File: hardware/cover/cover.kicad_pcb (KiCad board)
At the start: 2 copper layers, 35.5 x 41 mm, 5 parts, among them P101 CONN_02X03, SW101 SW_DIP_4

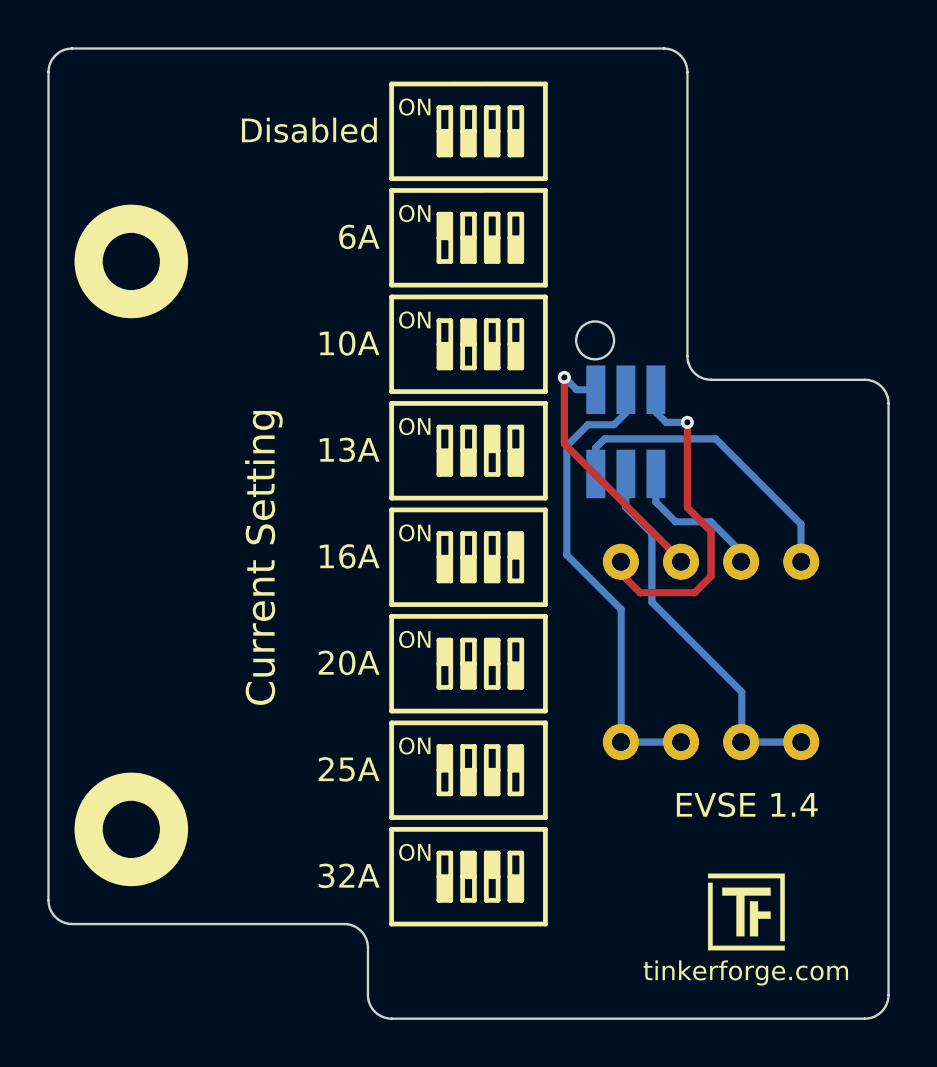
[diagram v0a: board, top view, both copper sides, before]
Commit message: decrease outline dimensions
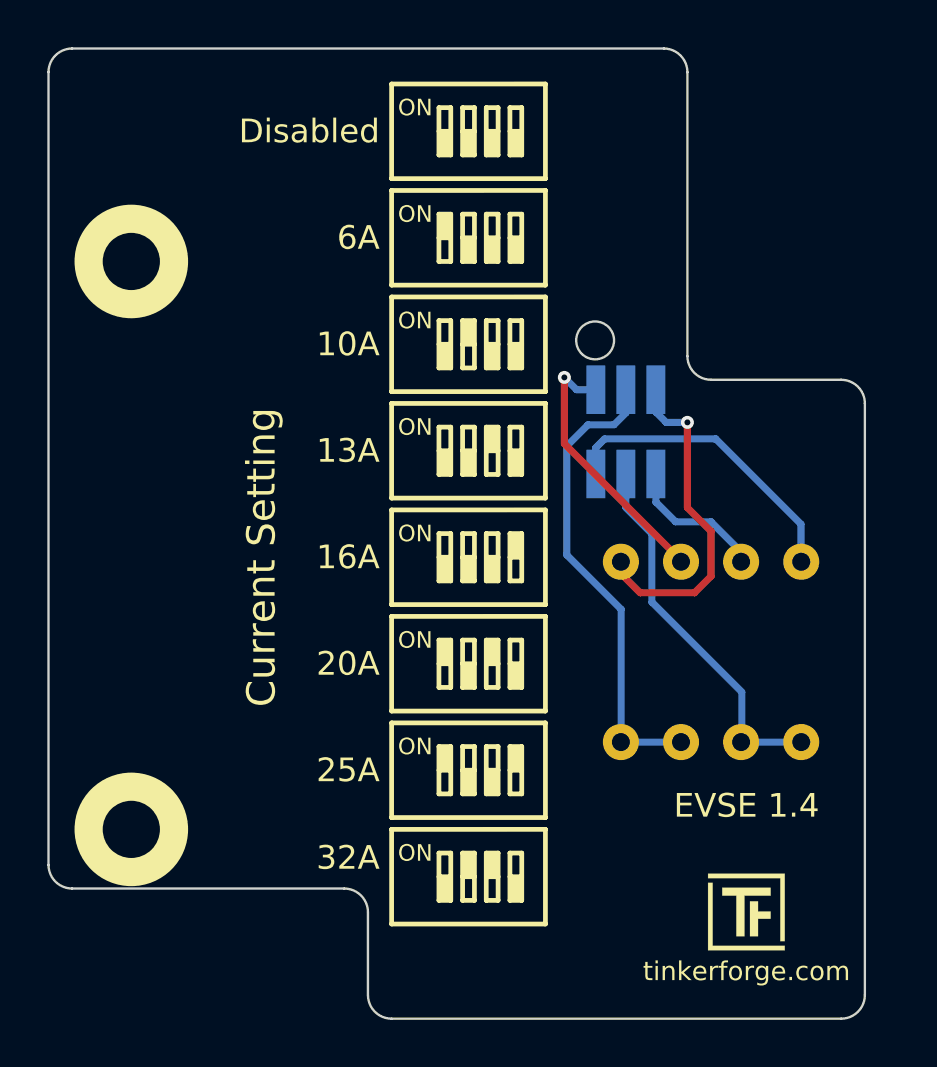
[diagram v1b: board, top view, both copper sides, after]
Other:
- board size 35.5 x 41 mm -> 34.5 x 41 mm
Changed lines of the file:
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@@
       (effects (font (size 0.1 0.1) (thickness 0.3)))
     )
-    (fp_poly (pts (xy -1.433286 1.42119) (xy 1.614714 1.42119) (xy 1.614714 1.608666) (xy -1.62681 1.608666)
-      (xy -1.62681 -1.239762) (xy -1.433286 -1.239762) (xy -1.433286 1.42119)) (layer F.SilkS) (width 0.01))
-    (fp_poly (pts (xy 1.614714 1.221619) (xy 1.427238 1.221619) (xy 1.427238 -1.439334) (xy -1.62681 -1.439334)
-      (xy -1.62681 -1.62681) (xy 1.614714 -1.62681) (xy 1.614714 1.221619)) (layer F.SilkS) (width 0.01))
+    (fp_poly (pts (xy 0.483809 -0.030238) (xy 1.016 -0.030238) (xy 1.016 0.27819) (xy 0.483809 0.27819)
+      (xy 0.483809 1.016) (xy 0.145142 1.016) (xy 0.145142 -0.459619) (xy 0.483809 -0.459619)
+      (xy 0.483809 -0.030238)) (layer F.SilkS) (width 0.01))
     (fp_poly (pts (xy 1.016 -0.701524) (xy -0.090715 -0.701524) (xy -0.090715 1.016) (xy -0.429381 1.016)
       (xy -0.429381 -0.701524) (xy -1.028096 -0.701524) (xy -1.028096 -1.034143) (xy 1.016 -1.034143)
       (xy 1.016 -0.701524)) (layer F.SilkS) (width 0.01))
-    (fp_poly (pts (xy 0.483809 -0.030238) (xy 1.016 -0.030238) (xy 1.016 0.27819) (xy 0.483809 0.27819)
-      (xy 0.483809 1.016) (xy 0.145142 1.016) (xy 0.145142 -0.459619) (xy 0.483809 -0.459619)
-      (xy 0.483809 -0.030238)) (layer F.SilkS) (width 0.01))
+    (fp_poly (pts (xy 1.614714 1.221619) (xy 1.427238 1.221619) (xy 1.427238 -1.439334) (xy -1.62681 -1.439334)
+      (xy -1.62681 -1.62681) (xy 1.614714 -1.62681) (xy 1.614714 1.221619)) (layer F.SilkS) (width 0.01))
+    (fp_poly (pts (xy -1.433286 1.42119) (xy 1.614714 1.42119) (xy 1.614714 1.608666) (xy -1.62681 1.608666)
+      (xy -1.62681 -1.239762) (xy -1.433286 -1.239762) (xy -1.433286 1.42119)) (layer F.SilkS) (width 0.01))
   )
   (module kicad-libraries:DRILL_NP (layer F.Cu)
@@
       (effects (font (size 0.29972 0.29972) (thickness 0.0762)))
     )
+    (fp_circle (center 0 0) (end 2.19964 0) (layer B.SilkS) (width 0.381))
+    (fp_circle (center 0 0) (end 1.89992 0) (layer B.SilkS) (width 0.381))
+    (fp_circle (center 0 0) (end 1.69926 0) (layer B.SilkS) (width 0.381))
+    (fp_circle (center 0 0) (end 1.39954 0) (layer F.SilkS) (width 0.381))
+    (fp_circle (center 0 0) (end 1.39954 -0.09906) (layer B.SilkS) (width 0.381))
+    (fp_circle (center 0 0) (end 1.69926 0) (layer F.SilkS) (width 0.381))
+    (fp_circle (center 0 0) (end 1.99898 -0.20066) (layer F.SilkS) (width 0.381))
+    (fp_circle (center 0 0) (end 2.19964 -0.20066) (layer F.SilkS) (width 0.381))
     (fp_circle (center 0 0) (end 3.2 0) (layer Eco2.User) (width 0.01))
-    (fp_circle (center 0 0) (end 2.19964 -0.20066) (layer F.SilkS) (width 0.381))
-    (fp_circle (center 0 0) (end 1.99898 -0.20066) (layer F.SilkS) (width 0.381))
-    (fp_circle (center 0 0) (end 1.69926 0) (layer F.SilkS) (width 0.381))
-    (fp_circle (center 0 0) (end 1.39954 -0.09906) (layer B.SilkS) (width 0.381))
-    (fp_circle (center 0 0) (end 1.39954 0) (layer F.SilkS) (width 0.381))
-    (fp_circle (center 0 0) (end 1.69926 0) (layer B.SilkS) (width 0.381))
-    (fp_circle (center 0 0) (end 1.89992 0) (layer B.SilkS) (width 0.381))
-    (fp_circle (center 0 0) (end 2.19964 0) (layer B.SilkS) (width 0.381))
     (pad "" np_thru_hole circle (at 0 0) (size 2.99974 2.99974) (drill 2.99974) (layers *.Cu *.Mask F.SilkS)
       (clearance 0.89916))
@@
       (effects (font (size 0.29972 0.29972) (thickness 0.0762)))
     )
+    (fp_circle (center 0 0) (end 2.19964 0) (layer B.SilkS) (width 0.381))
+    (fp_circle (center 0 0) (end 1.89992 0) (layer B.SilkS) (width 0.381))
+    (fp_circle (center 0 0) (end 1.69926 0) (layer B.SilkS) (width 0.381))
+    (fp_circle (center 0 0) (end 1.39954 0) (layer F.SilkS) (width 0.381))
+    (fp_circle (center 0 0) (end 1.39954 -0.09906) (layer B.SilkS) (width 0.381))
+    (fp_circle (center 0 0) (end 1.69926 0) (layer F.SilkS) (width 0.381))
+    (fp_circle (center 0 0) (end 1.99898 -0.20066) (layer F.SilkS) (width 0.381))
+    (fp_circle (center 0 0) (end 2.19964 -0.20066) (layer F.SilkS) (width 0.381))
     (fp_circle (center 0 0) (end 3.2 0) (layer Eco2.User) (width 0.01))
-    (fp_circle (center 0 0) (end 2.19964 -0.20066) (layer F.SilkS) (width 0.381))
-    (fp_circle (center 0 0) (end 1.99898 -0.20066) (layer F.SilkS) (width 0.381))
-    (fp_circle (center 0 0) (end 1.69926 0) (layer F.SilkS) (width 0.381))
-    (fp_circle (center 0 0) (end 1.39954 -0.09906) (layer B.SilkS) (width 0.381))
-    (fp_circle (center 0 0) (end 1.39954 0) (layer F.SilkS) (width 0.381))
-    (fp_circle (center 0 0) (end 1.69926 0) (layer B.SilkS) (width 0.381))
-    (fp_circle (center 0 0) (end 1.89992 0) (layer B.SilkS) (width 0.381))
-    (fp_circle (center 0 0) (end 2.19964 0) (layer B.SilkS) (width 0.381))
     (pad "" np_thru_hole circle (at 0 0) (size 2.99974 2.99974) (drill 2.99974) (layers *.Cu *.Mask F.SilkS)
       (clearance 0.89916))
@@
       (effects (font (size 0.15 0.15) (thickness 0.0375)) (justify mirror))
     )
+    (fp_circle (center -1.2 1) (end -0.883772 1) (layer B.Fab) (width 0.1))
+    (fp_line (start -2.2 -1.5) (end -2.2 1.5) (layer B.Fab) (width 0.1))
+    (fp_line (start 2.2 -1.5) (end -2.2 -1.5) (layer B.Fab) (width 0.1))
+    (fp_line (start 2.2 1.5) (end 2.2 -1.5) (layer B.Fab) (width 0.1))
     (fp_line (start -2.2 1.5) (end 2.2 1.5) (layer B.Fab) (width 0.1))
-    (fp_line (start 2.2 1.5) (end 2.2 -1.5) (layer B.Fab) (width 0.1))
-    (fp_line (start 2.2 -1.5) (end -2.2 -1.5) (layer B.Fab) (width 0.1))
-    (fp_line (start -2.2 -1.5) (end -2.2 1.5) (layer B.Fab) (width 0.1))
-    (fp_circle (center -1.2 1) (end -0.883772 1) (layer B.Fab) (width 0.1))
     (pad 1 smd rect (at -1.27 1.78) (size 0.8 2.05) (layers B.Cu B.Paste B.Mask)
       (net 1 "Net-(P101-Pad1)"))
@@
       (effects (font (size 0.3 0.3) (thickness 0.075)))
     )
+    (fp_line (start -6.2 4.9) (end -6.2 -4.9) (layer F.Fab) (width 0.05))
+    (fp_line (start 6.2 4.9) (end -6.2 4.9) (layer F.Fab) (width 0.05))
+    (fp_line (start 6.2 -4.9) (end 6.2 4.9) (layer F.Fab) (width 0.05))
     (fp_line (start -6.2 -4.9) (end 6.2 -4.9) (layer F.Fab) (width 0.05))
-    (fp_line (start 6.2 -4.9) (end 6.2 4.9) (layer F.Fab) (width 0.05))
-    (fp_line (start 6.2 4.9) (end -6.2 4.9) (layer F.Fab) (width 0.05))
-    (fp_line (start -6.2 4.9) (end -6.2 -4.9) (layer F.Fab) (width 0.05))
     (pad 1 thru_hole circle (at -3.81 3.81 180) (size 1.524 1.524) (drill 0.762) (layers *.Cu *.Mask F.SilkS)
       (net 1 "Net-(P101-Pad1)"))
@@
     (effects (font (size 1.2 1.2) (thickness 0.2)))
   )
-  (gr_arc (start 173.5 108.15) (end 173.5 109.15) (angle -90) (layer Edge.Cuts) (width 0.09906))
+  (gr_arc (start 172.5 108.15) (end 172.5 109.15) (angle -90) (layer Edge.Cuts) (width 0.09906))
   (gr_arc (start 153.5 108.15) (end 152.5 108.15) (angle -90) (layer Edge.Cuts) (width 0.09906))
-  (gr_line (start 153.5 109.15) (end 173.5 109.15) (layer Edge.Cuts) (width 0.09906))
+  (gr_line (start 153.5 109.15) (end 172.5 109.15) (layer Edge.Cuts) (width 0.09906))
   (gr_line (start 181.5 119.65) (end 139 119.65) (layer Dwgs.User) (width 0.09906))
-  (gr_text 32A (at 153 103.15) (layer F.SilkS)
+  (gr_text 32A (at 153 102.35) (layer F.SilkS)
     (effects (font (size 1 1) (thickness 0.15)) (justify right))
   )
@@
   (gr_circle (center 162.1 80.485493) (end 162.9 80.485493) (layer Edge.Cuts) (width 0.09906))
   (gr_circle (center 163.4 84.35) (end 163.5 84.35) (layer Dwgs.User) (width 0.15))
-  (gr_line (start 152.5 106.15) (end 152.5 108.15) (layer Edge.Cuts) (width 0.09906))
-  (gr_line (start 140 105.15) (end 151.5 105.15) (layer Edge.Cuts) (width 0.09906))
-  (gr_line (start 139 69.15) (end 139 104.15) (layer Edge.Cuts) (width 0.09906))
+  (gr_line (start 152.5 104.65) (end 152.5 108.15) (layer Edge.Cuts) (width 0.09906))
+  (gr_line (start 140 103.65) (end 151.5 103.65) (layer Edge.Cuts) (width 0.09906))
+  (gr_line (start 139 69.15) (end 139 102.65) (layer Edge.Cuts) (width 0.09906))
   (gr_line (start 165 68.15) (end 140 68.15) (layer Edge.Cuts) (width 0.09906))
   (gr_line (start 166 81.15) (end 166 69.15) (layer Edge.Cuts) (width 0.09906))
-  (gr_line (start 173.5 82.15) (end 167 82.15) (layer Edge.Cuts) (width 0.09906))
-  (gr_line (start 174.5 108.15) (end 174.5 83.15) (layer Edge.Cuts) (width 0.09906))
-  (gr_arc (start 173.5 83.15) (end 174.5 83.15) (angle -90) (layer Edge.Cuts) (width 0.09906))
+  (gr_line (start 172.5 82.15) (end 167 82.15) (layer Edge.Cuts) (width 0.09906))
+  (gr_line (start 173.5 108.15) (end 173.5 83.15) (layer Edge.Cuts) (width 0.09906))
+  (gr_arc (start 172.5 83.15) (end 173.5 83.15) (angle -90) (layer Edge.Cuts) (width 0.09906))
   (gr_arc (start 167 81.15) (end 166 81.15) (angle -90) (layer Edge.Cuts) (width 0.09906))
   (gr_arc (start 165 69.15) (end 166 69.15) (angle -90) (layer Edge.Cuts) (width 0.09906))
   (gr_arc (start 140 69.15) (end 140 68.15) (angle -90) (layer Edge.Cuts) (width 0.09906))
-  (gr_arc (start 140 104.15) (end 139 104.15) (angle -90) (layer Edge.Cuts) (width 0.09906))
-  (gr_arc (start 151.5 106.15) (end 152.5 106.15) (angle -90) (layer Edge.Cuts) (width 0.09906))
+  (gr_arc (start 140 102.65) (end 139 102.65) (angle -90) (layer Edge.Cuts) (width 0.09906))
+  (gr_arc (start 151.5 104.65) (end 152.5 104.65) (angle -90) (layer Edge.Cuts) (width 0.09906))
   (gr_text tinkerforge.com (at 168.5 107.15) (layer F.SilkS)
     (effects (font (size 0.8 0.8) (thickness 0.15)))

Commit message: change cover to two single switch design, change current setting!!!!
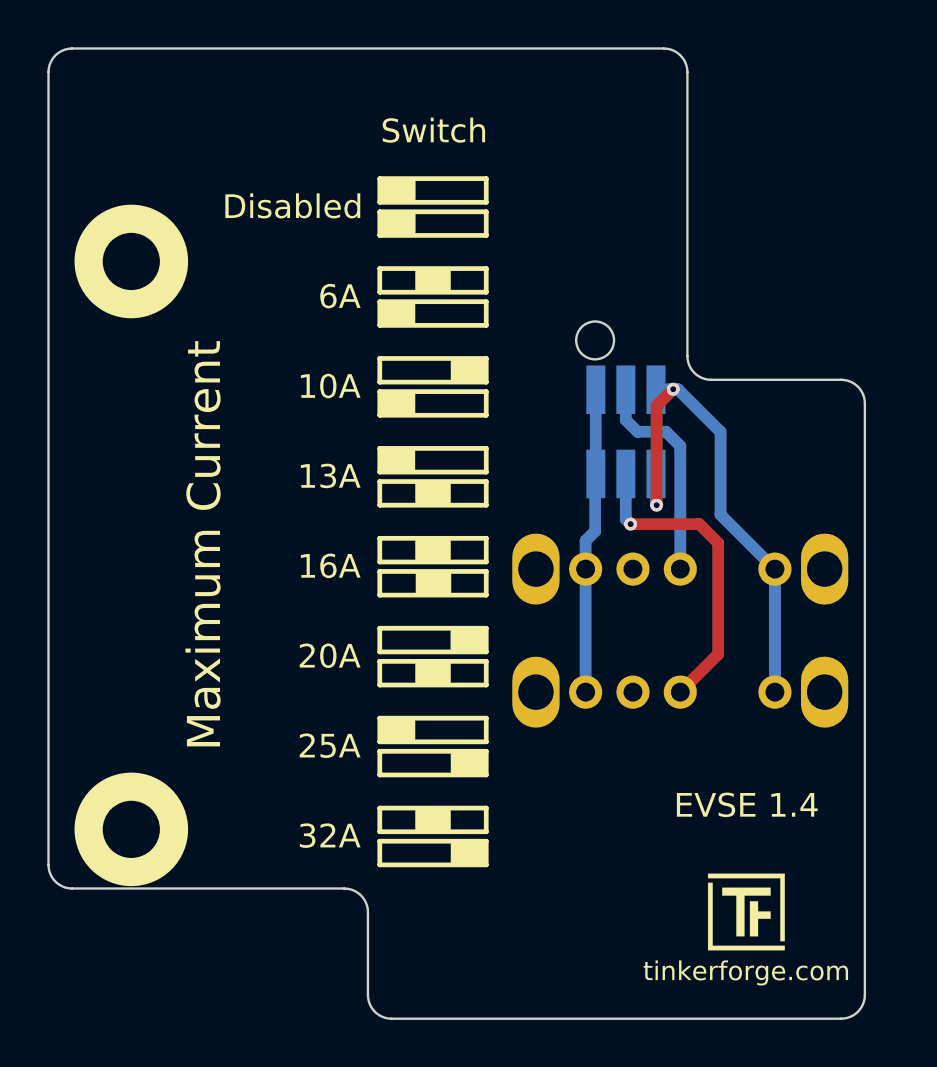
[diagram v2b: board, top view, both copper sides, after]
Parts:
- added SW102: OS103011MS8QP1, kicad-libraries:OS103011MS8QP1, F.Cu at (165.7, 95.3)
- SW101: value SW_DIP_4 -> OS103011MS8QP1; footprint kicad-libraries:SW_DIP_4_THT -> kicad-libraries:OS103011MS8QP1
- moved SW101 3.73 mm to (165.7, 90.2)
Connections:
- P101 pad 1: Net-(P101-Pad1) -> 3V3
- P101 pad 2: Net-(P101-Pad2) -> 3V3
- P101 pad 5: Net-(P101-Pad5) -> GND
- P101 pad 6: Net-(P101-Pad6) -> GND
- SW101 pad 1: Net-(P101-Pad1) -> GND
- SW101 pad 2: Net-(P101-Pad5) -> Net-(P101-Pad4)
- SW101 pad 3: Net-(P101-Pad2) -> Net-(SW101-Pad3)
- SW101 pad 4: Net-(P101-Pad6) -> 3V3
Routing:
- net GND: track 0.00 -> 22.7 mm, vias 0 -> 2
- net Net-(P101-Pad6): track 15.1 -> 0.00 mm, vias 1 -> 0
- net Net-(P101-Pad1): track 13.1 -> 0.00 mm
- net 3V3: track 0.00 -> 13.0 mm
- net Net-(P101-Pad2): track 11.4 -> 0.00 mm, vias 1 -> 0
- net Net-(P101-Pad4): track 19.9 -> 9.26 mm
- net Net-(P101-Pad5): track 6.10 -> 0.00 mm
- net Net-(P101-Pad3): track 16.0 -> 13.2 mm, vias 0 -> 1
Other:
- board text added: "1"
- board text added: "2"
- board text added: "3V3"
- board text added: "DNC"
- board text added: "GND"
- board text added: "Maximum Current"
- board text added: "PIN0 = P0_0"
- board text added: "PIN1 = P0_5"
- board text added: "Switch"
- board text removed: "Current Setting"
- board text removed: "ON"
